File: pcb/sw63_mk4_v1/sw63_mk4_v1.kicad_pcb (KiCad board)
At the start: 4 copper layers, 35 x 35 mm, 68 parts, among them J1 USB_C_Receptacle_USB2.0_16P, J2 SWD, J3 Conn_01x02, Q1 DMG2305UX-7, Q2 DMG2302U-7, Q3 TEMT6200FX01, SW1 KSC321J LFS, SW2 ﻿EVQ-P7J01P, U1 DIO5518BST5, U2 MCP1711T-3.3I/OT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

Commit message: routing, graphics
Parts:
- J1: value USB_C_Receptacle_USB2.0_16P -> GT-USB-7070C
- U3, U4, U5: value TLC5916 -> TLC5916IPWR
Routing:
- net GND: track 33.6 -> 37.1 mm, vias 25 -> 26
- net /VSEL: track 137.8 -> 138.6 mm
- net Net-(D16-K): track 14.3 -> 14.9 mm
- net Net-(D15-K): track 6.35 -> 6.87 mm
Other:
- board text added: "H"
- board text added: "M"
- board text added: "P"

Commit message: updated models
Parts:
- Q3: footprint Diode_SMD:D_0805_2012Metric -> sw63_mk4:TEMT6200FX01
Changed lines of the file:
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@@
 		)
 	)
-	(footprint "Diode_SMD:D_0805_2012Metric"
+	(footprint "sw63_mk4:TEMT6200FX01"
 		(layer "F.Cu")
 		(at 121.6 86.6)
@@
 		(attr smd)
 		(fp_line
-			(start -1.685 -0.96)
-			(end -1.685 0.96)
-			(stroke
-				(width 0.12)
-				(type solid)
-			)
-			(layer "F.SilkS")
-		)
-		(fp_line
-			(start -1.685 0.96)
-			(end 1 0.96)
-			(stroke
-				(width 0.12)
-				(type solid)
-			)
-			(layer "F.SilkS")
-		)
-		(fp_line
-			(start 1 -0.96)
-			(end -1.685 -0.96)
-			(stroke
-				(width 0.12)
-				(type solid)
-			)
+			(start -0.4 0)
+			(end -0.2 0)
+			(stroke
+				(width 0.1)
+				(type default)
+			)
+			(layer "F.SilkS")
+		)
+		(fp_line
+			(start -0.2 0)
+			(end -0.2 0.2)
+			(stroke
+				(width 0.1)
+				(type default)
+			)
+			(layer "F.SilkS")
+		)
+		(fp_line
+			(start 0 0.2)
+			(end 0 0)
+			(stroke
+				(width 0.1)
+				(type default)
+			)
+			(layer "F.SilkS")
+		)
+		(fp_line
+			(start 0.2 -0.2)
+			(end 0.2 0.2)
+			(stroke
+				(width 0.1)
+				(type default)
+			)
+			(layer "F.SilkS")
+		)
+		(fp_line
+			(start 0.2 -0.2)
+			(end 0.4 0)
+			(stroke
+				(width 0.1)
+				(type default)
+			)
+			(layer "F.SilkS")
+		)
+		(fp_line
+			(start 0.2 0.2)
+			(end 0.4 0)
+			(stroke
+				(width 0.1)
+				(type default)
+			)
+			(layer "F.SilkS")
+		)
+		(fp_line
+			(start 0.25 -0.15)
+			(end 0.25 0.1)
+			(stroke
+				(width 0.1)
+				(type default)
+			)
+			(layer "F.SilkS")
+		)
+		(fp_line
+			(start 0.4 0)
+			(end 0 0)
+			(stroke
+				(width 0.1)
+				(type default)
+			)
+			(layer "F.SilkS")
+		)
+		(fp_rect
+			(start -0.25 0.2)
+			(end 0.05 0.275)
+			(stroke
+				(width 0.1)
+				(type default)
+			)
+			(fill no)
 			(layer "F.SilkS")
 		)
@@
 		)
 		(embedded_fonts no)
-		(model "${KICAD9_3DMODEL_DIR}/Diode_SMD.3dshapes/D_0805_2012Metric.step"
+		(model "${KICAD9_3DMODEL_DIR}/LED_SMD.3dshapes/LED_0805_2012Metric.step"
 			(offset
 				(xyz 0 0 0)

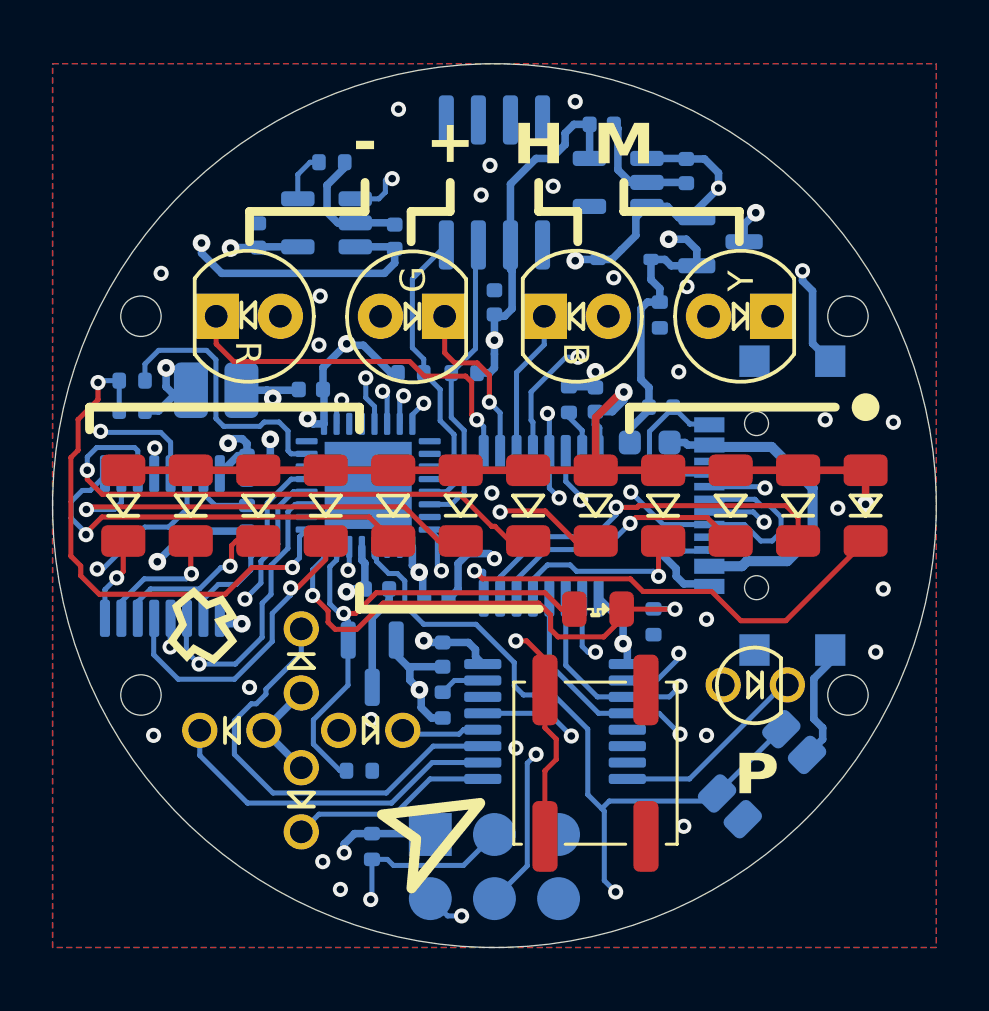
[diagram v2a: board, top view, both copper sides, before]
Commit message: add usb dtct
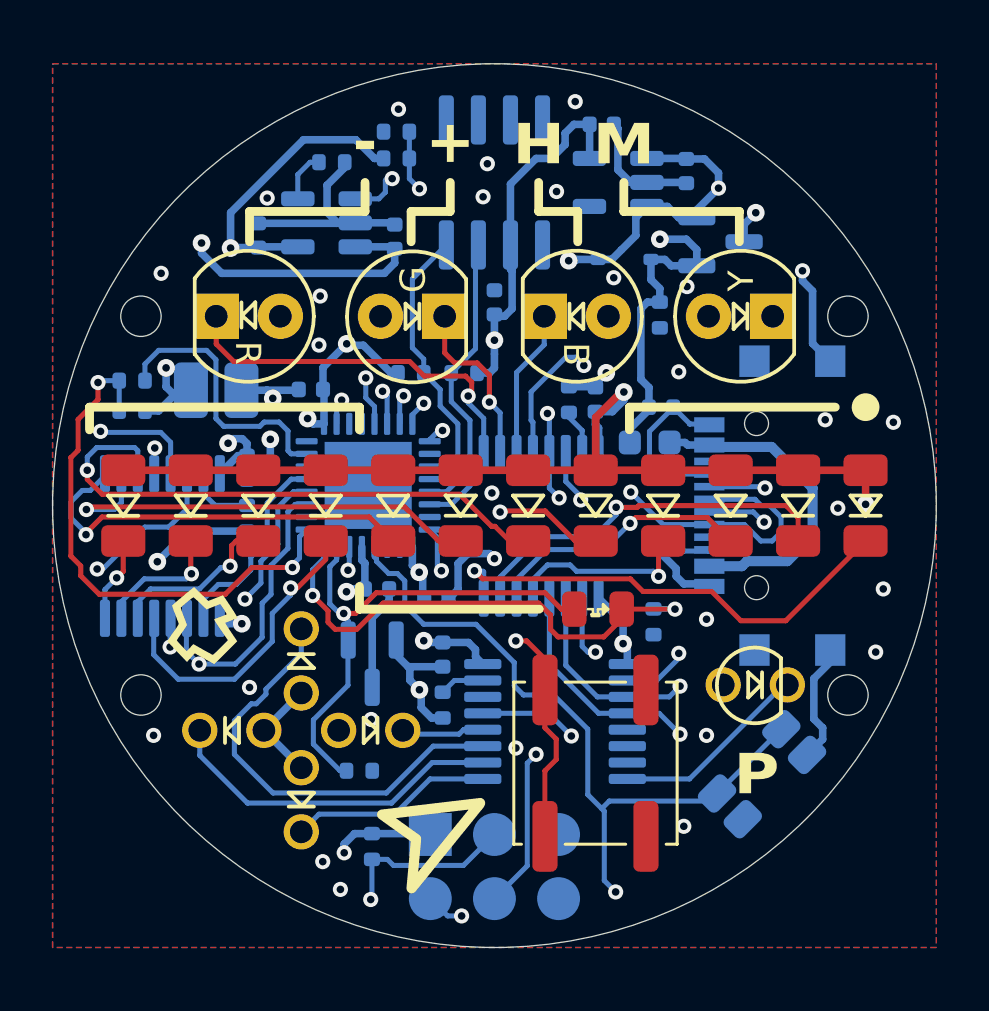
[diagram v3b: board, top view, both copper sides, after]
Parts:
- added R15: 22k, Resistor_SMD:R_0402_1005Metric, B.Cu at (113.6, 68.8)
- added R16: 22k, Resistor_SMD:R_0402_1005Metric, B.Cu at (113.6, 67.7)
- R10, R9: value 4k7 -> 5k1
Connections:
- U7 pad 25: unconnected-(U7-PA15-Pad25) -> /USB_DTCT
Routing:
- net /USB_DTCT: track 0.00 -> 32.6 mm, vias 0 -> 2
- net VBUS: track 33.2 -> 42.2 mm
- net GND: track 37.1 -> 40.3 mm, vias 26 -> 27
- net /GND_LED: track 62.6 -> 64.0 mm
- net /VSEL: track 138.6 -> 137.8 mm
- net VDD: track 78.5 -> 78.0 mm

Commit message: update board
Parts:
- moved J1 0.50 mm to (131.3, 82.5)
- moved D21 0.14 mm to (129.2, 89.7)
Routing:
- net GND: track 40.3 -> 37.4 mm
- net Net-(F1-Pad1): track 13.0 -> 11.9 mm
- net /D-: track 26.6 -> 25.6 mm
- net Net-(J1-CC1): track 1.35 -> 1.85 mm
- net /D+: track 24.8 -> 24.3 mm

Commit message: panelization prepare
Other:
- board size 35 x 35 mm -> 35.1 x 36 mm
